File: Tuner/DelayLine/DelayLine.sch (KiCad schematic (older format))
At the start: 84 parts, among them J1 Conn_Coaxial, J10 Conn_Coaxial, J11 Conn_Coaxial, J12 Conn_Coaxial, J13 Conn_01x01, J14 Conn_01x01, J15 Conn_01x01, J16 Conn_01x01, J17 Conn_02x10_Odd_Even, J18 Conn_Coaxial, J19 Conn_Coaxial, J2 Conn_Coaxial, J20 Conn_Coaxial, J21 Conn_Coaxial, J22 Conn_Coaxial, J23 Conn_Coaxial, J24 Conn_Coaxial, J25 Conn_01x01, J26 Conn_01x01, J27 Conn_01x01, J28 Conn_01x01, J29 Conn_Coaxial, J3 Conn_Coaxial, J30 Conn_Coaxial, J31 Conn_Coaxial, J4 Conn_Coaxial, J5 Conn_Coaxial, J6 Conn_Coaxial, J7 Conn_Coaxial, J8 Conn_01x02, J9 Conn_01x02

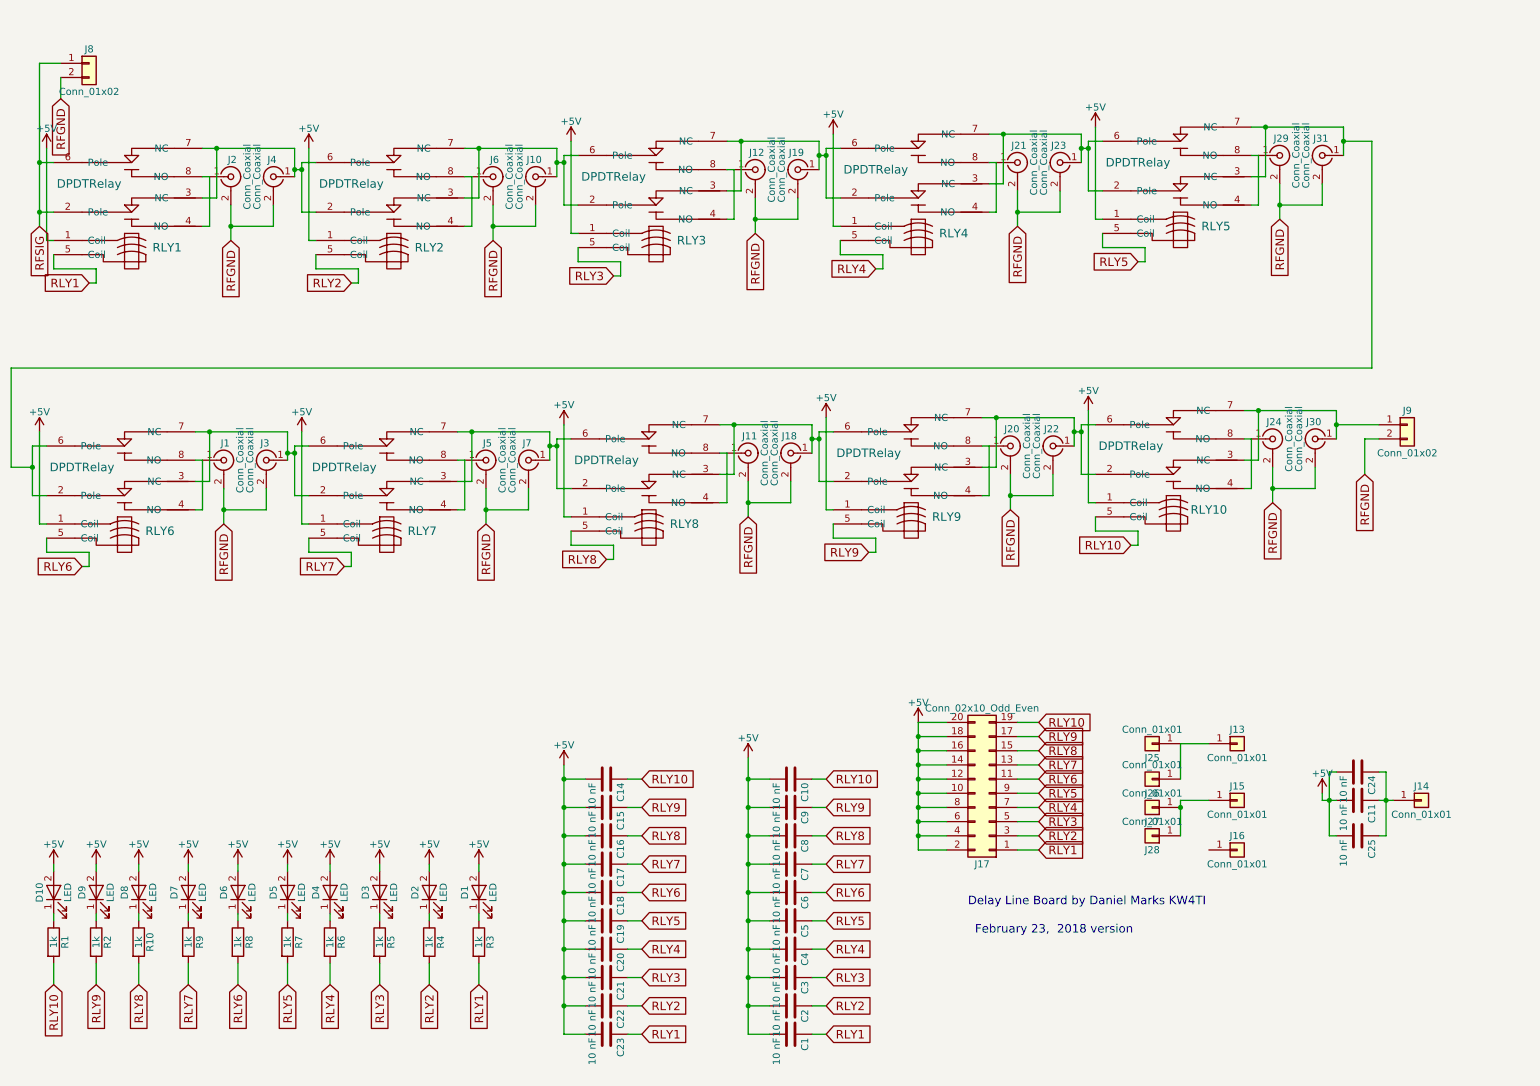
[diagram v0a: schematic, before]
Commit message: Added phase reversal transformer
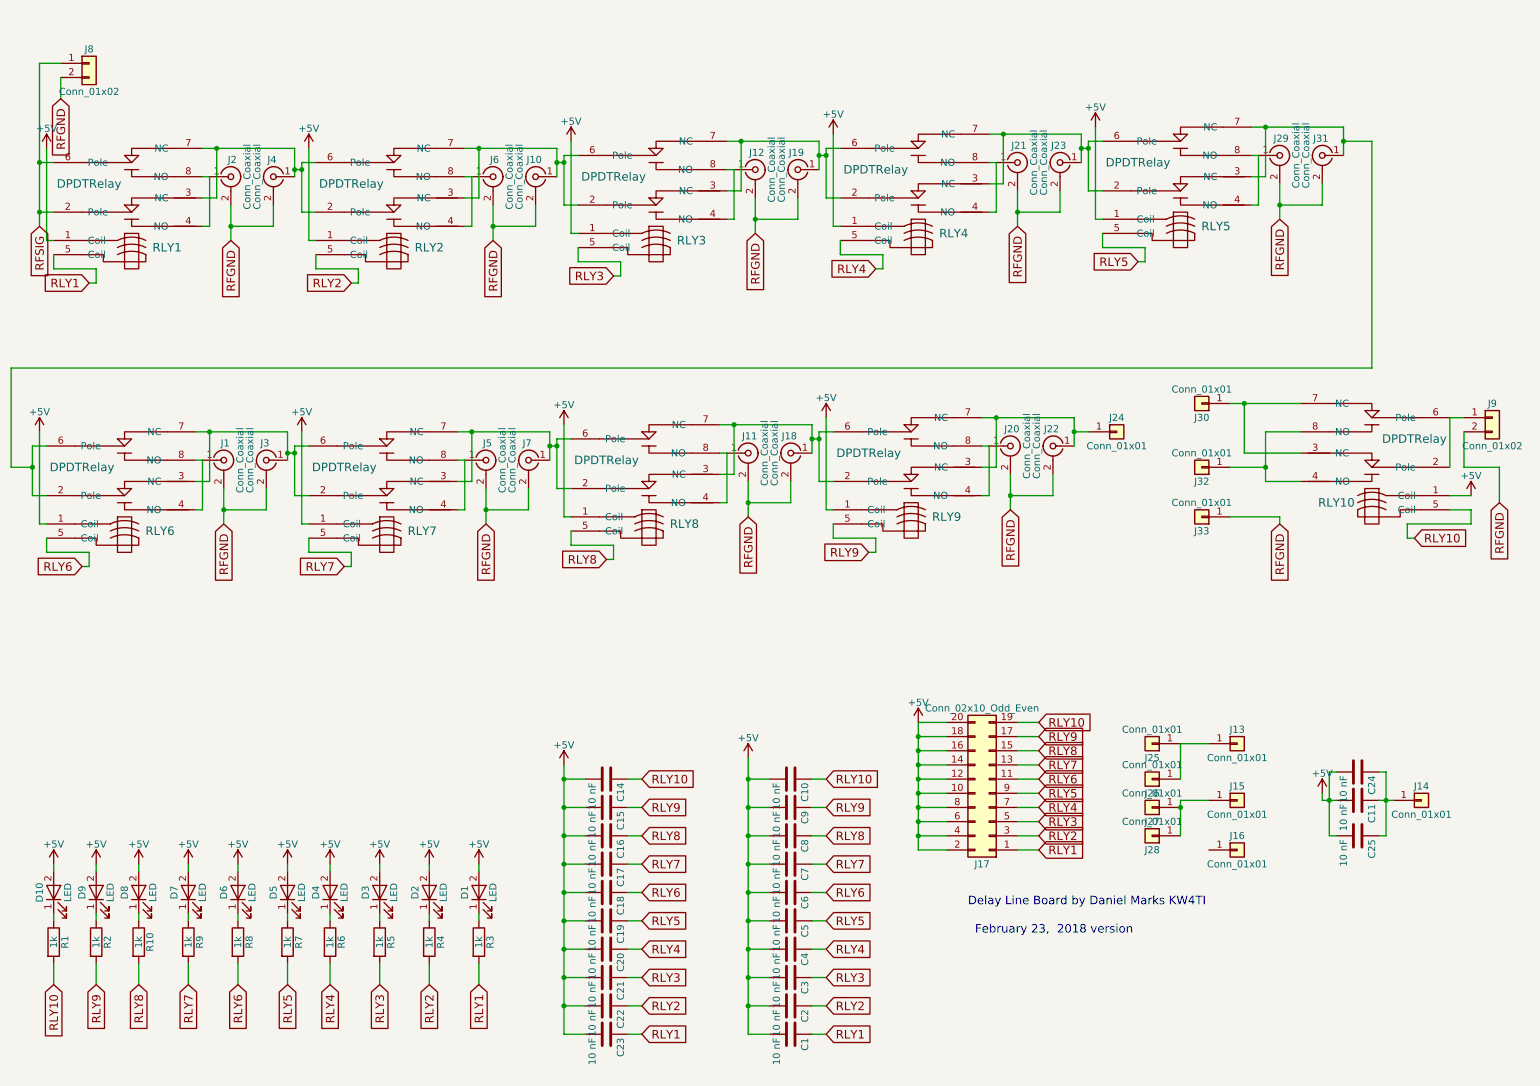
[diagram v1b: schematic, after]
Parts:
- removed J24, J30: Conn_Coaxial, Connectors:bnc-ci, symbol Conn_Coaxial
- added J24, J30, J32, J33: Conn_01x01, Connectors:1pin, symbol Conn_01x01
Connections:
- net RFGND: now also J33.1 (Pin_1)
- net at RLY10.3 (NC), RLY10.7 (NC): now also J30.1 (Pin_1); no longer J9.1 (Pin_1)
- net at J22.1 (In), RLY9.3 (NC), RLY9.7 (NC): now also J24.1 (Pin_1); no longer RLY10.2 (Pole), RLY10.6 (Pole)
- net at RLY10.4 (NO), RLY10.8 (NO): now also J32.1 (Pin_1)
- new net: J9.1 (Pin_1), RLY10.2 (Pole), RLY10.6 (Pole)
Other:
- moved on the sheet: J9, RLY10

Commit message: Added Quad Coupler
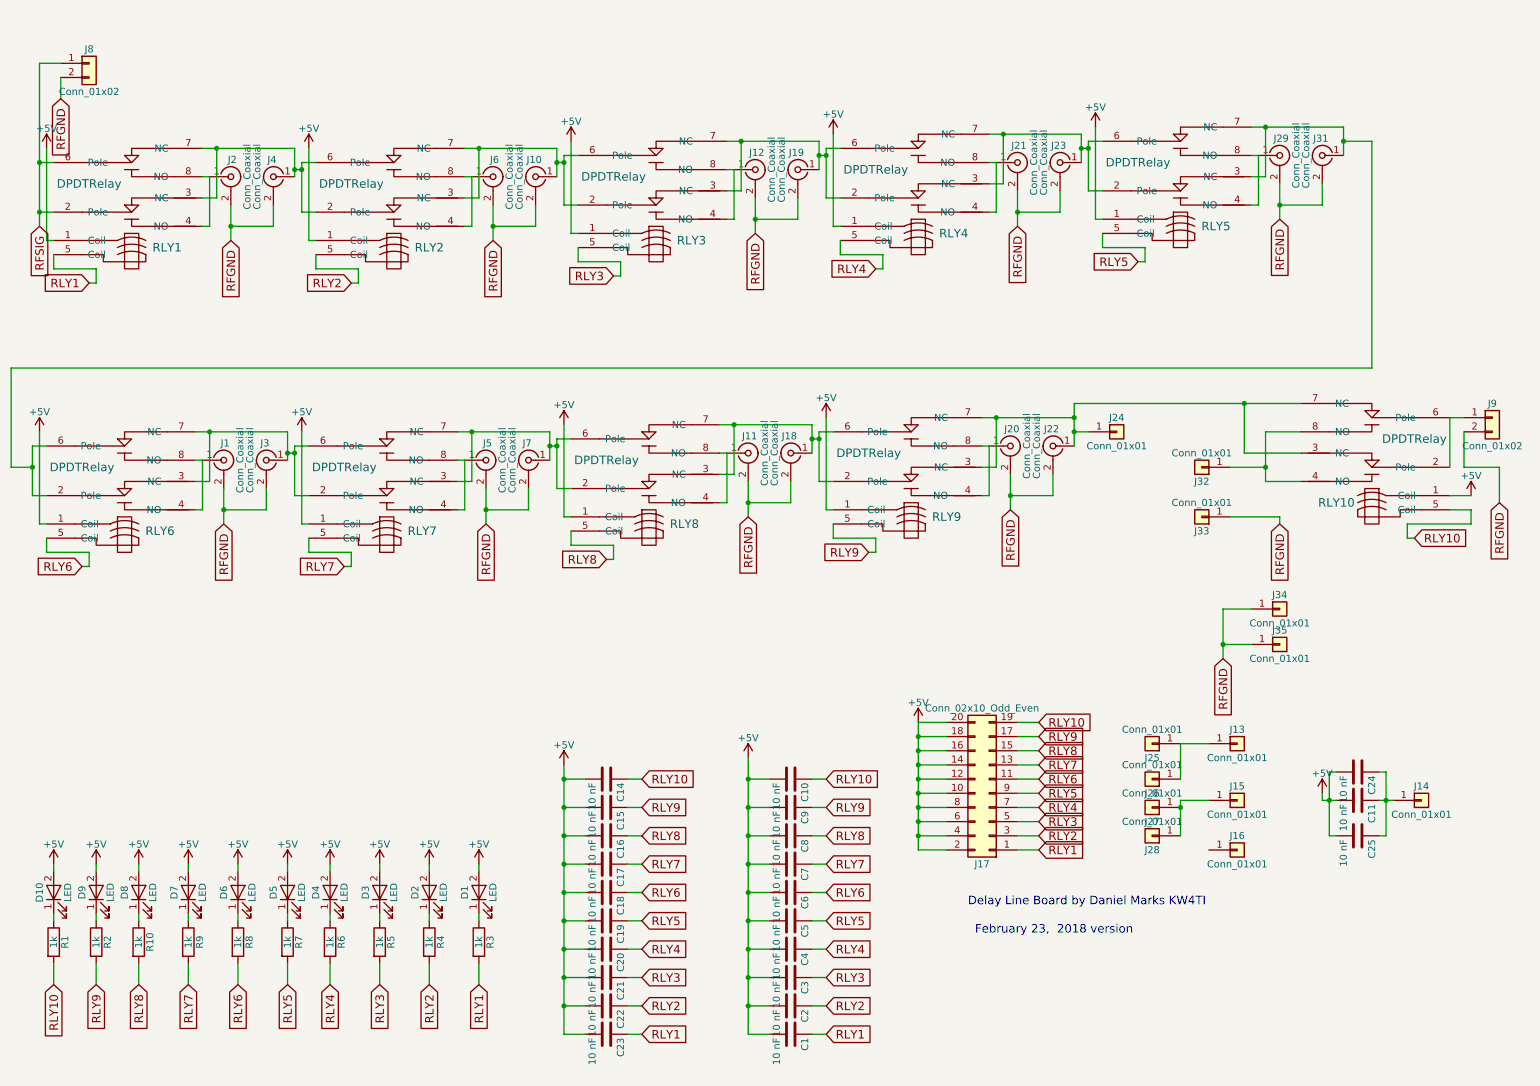
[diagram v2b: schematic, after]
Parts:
- removed J30: Conn_01x01, Connectors:1pin, symbol Conn_01x01
- added J34, J35: Conn_01x01, tuner:SOLDERJUMPER, symbol Conn_01x01
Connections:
- net RFGND: now also J34.1 (Pin_1), J35.1 (Pin_1)
- net at J22.1 (In), J24.1 (Pin_1), RLY9.3 (NC)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: now also RLY10.3 (NC), RLY10.7 (NC)

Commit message: Modified DelayLine to include bypass control
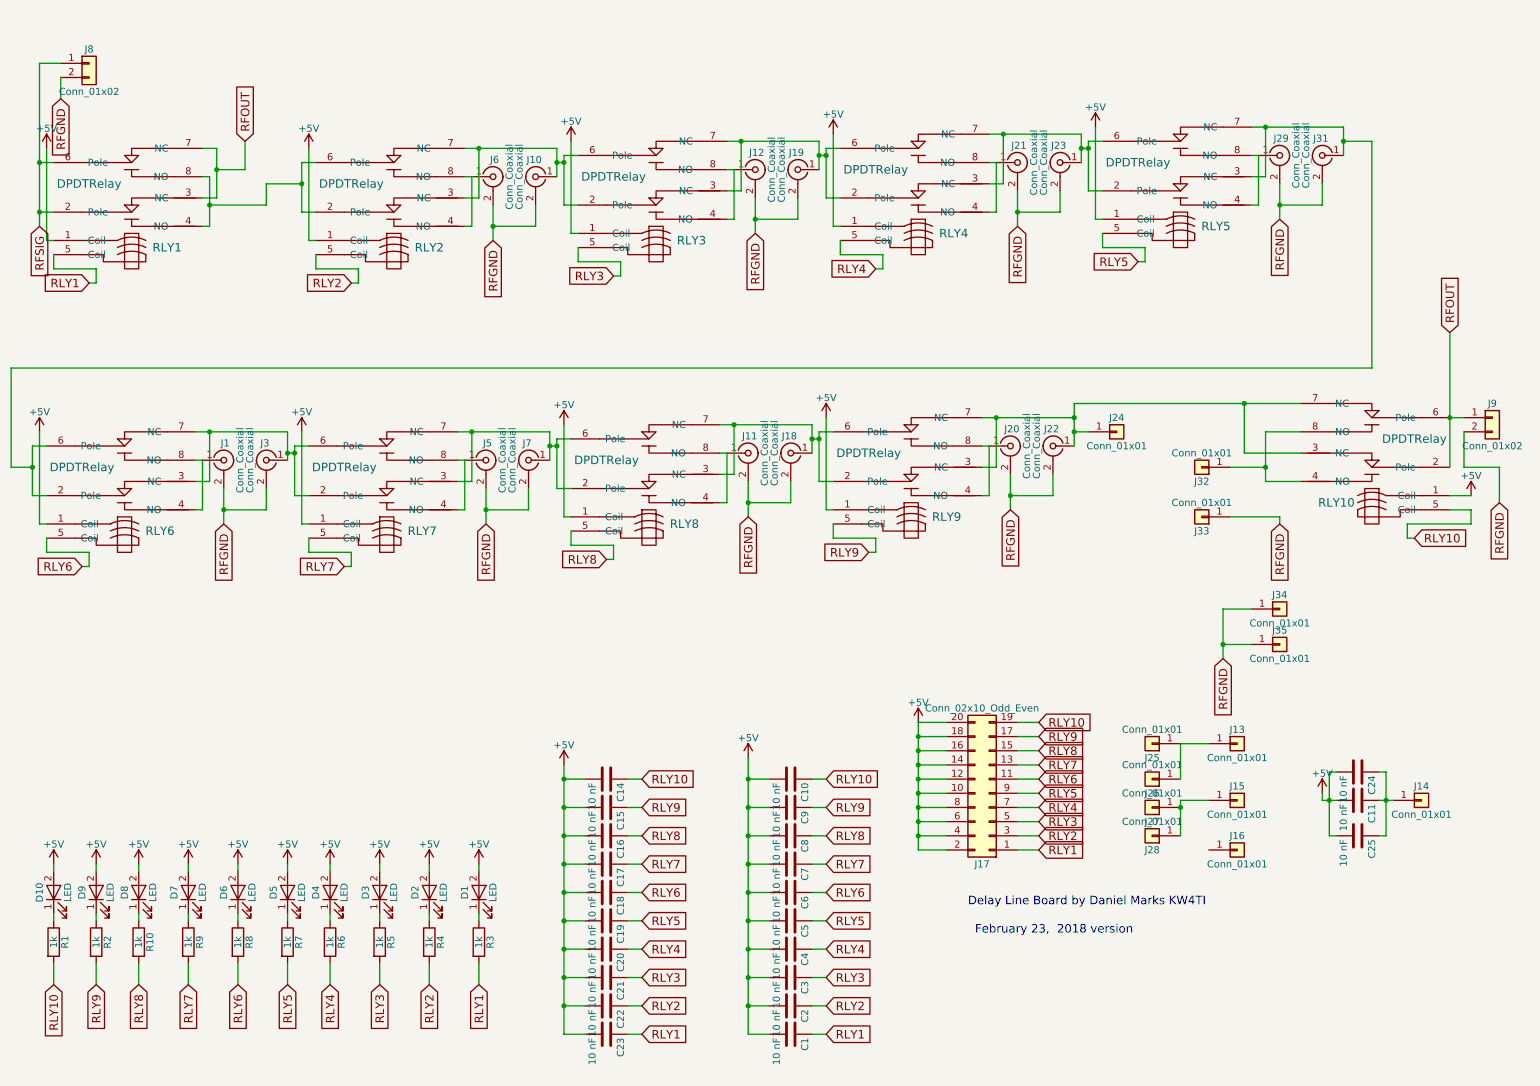
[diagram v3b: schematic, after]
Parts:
- removed J2, J4: Conn_Coaxial, Connectors:bnc-ci, symbol Conn_Coaxial
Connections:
- net RFOUT: now reaches J9.1 (Pin_1), RLY10.2 (Pole), RLY10.6 (Pole)
- net RFOUT: now also RLY1.3 (NC), RLY1.7 (NC)
- net at RLY2.2 (Pole), RLY2.6 (Pole): now also RLY1.4 (NO), RLY1.8 (NO); no longer RLY1.3 (NC), RLY1.7 (NC)
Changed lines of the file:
@@
 	1    0    0    -1
 $EndComp
-$Comp
-L Conn_Coaxial J2
-U 1 1 5C72CAE2
-P 2100 1550
-F 0 "J2" H 2110 1670 50  0000 C CNN
-F 1 "Conn_Coaxial" V 2215 1550 50  0000 C CNN
-F 2 "Connectors:bnc-ci" H 2100 1550 50  0001 C CNN
-F 3 "" H 2100 1550 50  0001 C CNN
-	1    2100 1550
-	1    0    0    -1
-$EndComp
-$Comp
-L Conn_Coaxial J4
-U 1 1 5C72CCE7
-P 2400 1550
-F 0 "J4" H 2410 1670 50  0000 C CNN
-F 1 "Conn_Coaxial" V 2515 1550 50  0000 C CNN
-F 2 "Connectors:bnc-ci" H 2400 1550 50  0001 C CNN
-F 3 "" H 2400 1550 50  0001 C CNN
-	1    2400 1550
-	-1   0    0    -1
-$EndComp
-Text GLabel 2100 2000 3    60   Input ~ 0
-RFGND
 Text GLabel 2950 2300 0    60   Input ~ 0
 RLY2
@@
 Text GLabel 9500 4000 3    60   Input ~ 0
 RFGND
-Connection ~ 2100 1900
-Wire Wire Line
-	2400 1900 2400 1750
-Wire Wire Line
-	2100 1900 2400 1900
-Wire Wire Line
-	2100 1750 2100 2000
 Wire Wire Line
 	750  1800 850  1800
@@
 	2000 1700 2000 1350
 Wire Wire Line
-	1900 1350 2550 1350
+	2000 1350 1900 1350
 Wire Wire Line
 	1950 1550 1900 1550
@@
 Wire Wire Line
 	1950 1900 1900 1900
-Wire Wire Line
-	2550 1350 2550 1550
-Connection ~ 2000 1350
 Wire Wire Line
 	800  1350 800  2000
@@
 Wire Wire Line
 	2600 1450 2600 1800
-Wire Wire Line
-	2600 1500 2550 1500
-Connection ~ 2550 1500
-Connection ~ 2600 1500
 Connection ~ 5800 1850
 Wire Wire Line
@@
 	10800 3600 10800 3350
 Wire Wire Line
-	10700 3600 10700 3250
+	10700 2650 10700 3600
 Wire Wire Line
 	10700 3250 10800 3250
@@
 Connection ~ 9100 4850
 Connection ~ 8050 3250
+Text GLabel 10700 2650 1    60   Input ~ 0
+RFOUT
+Connection ~ 10700 3250
+Wire Wire Line
+	1950 1750 2350 1750
+Wire Wire Line
+	2350 1750 2350 1600
+Wire Wire Line
+	2350 1600 2600 1600
+Connection ~ 2600 1600
+Connection ~ 1950 1750
+Text GLabel 2200 1300 1    60   Input ~ 0
+RFOUT
+Wire Wire Line
+	2200 1300 2200 1500
+Wire Wire Line
+	2200 1500 2000 1500
+Connection ~ 2000 1500
 $EndSCHEMATC

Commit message: Changed DelayLine to short out sections
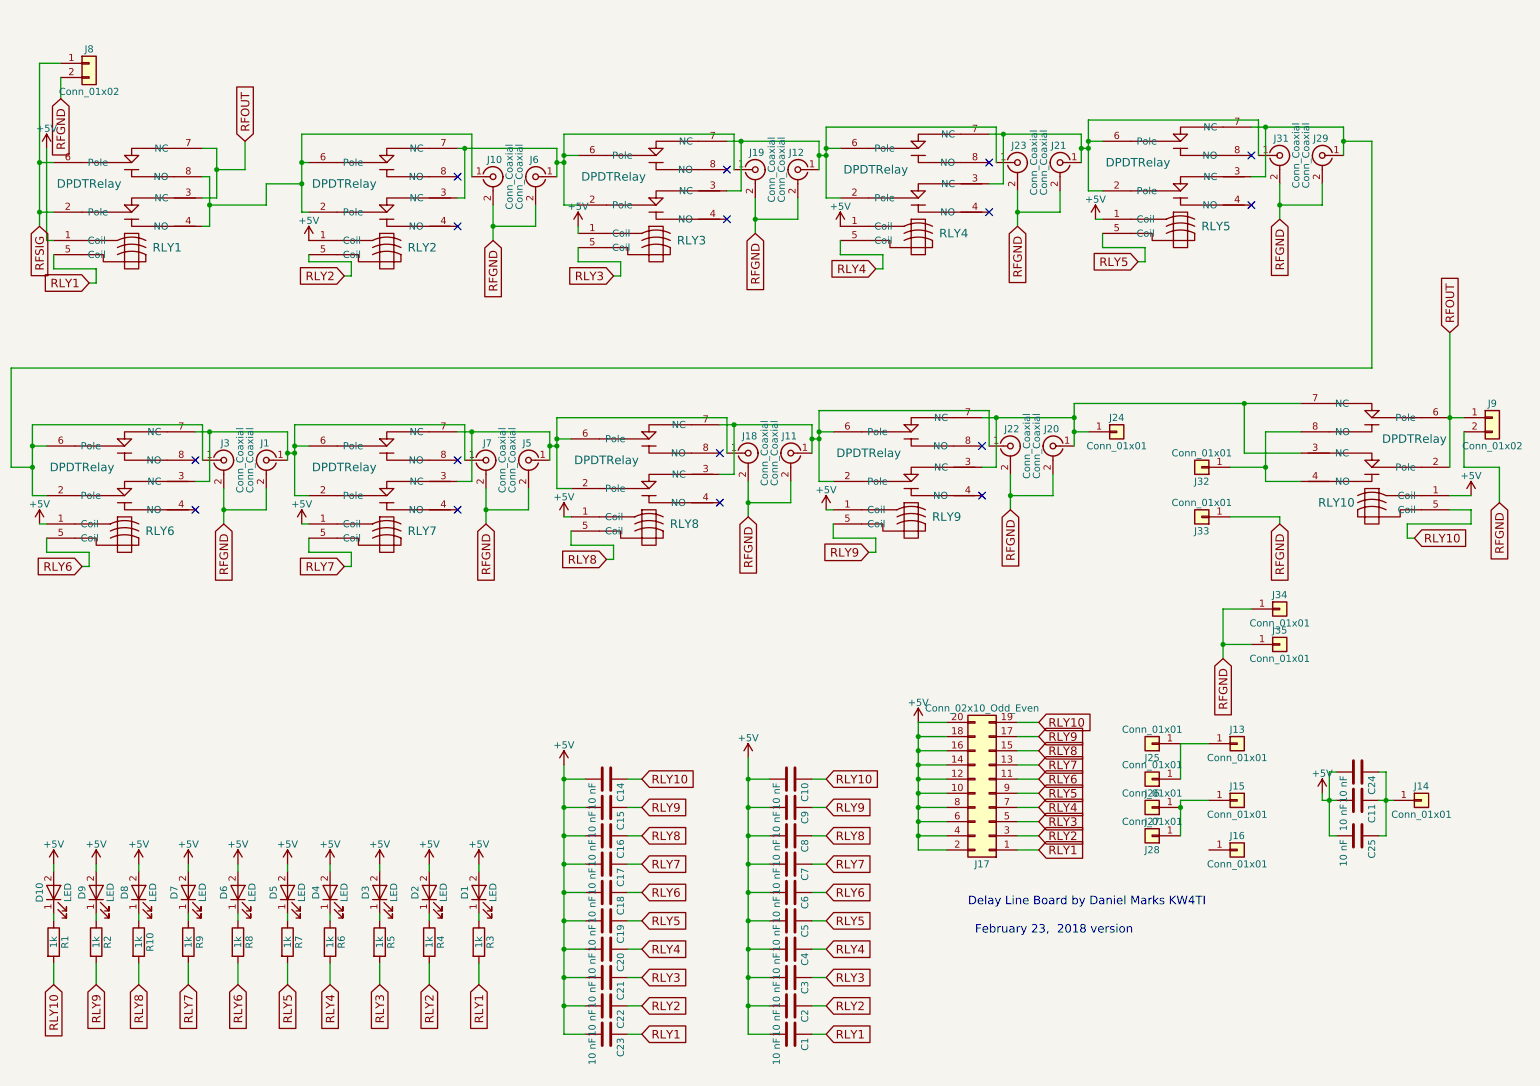
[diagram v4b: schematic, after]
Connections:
- net at RLY1.4 (NO), RLY1.8 (NO), RLY2.2 (Pole)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: now also J10.1 (In)
- net at J24.1 (Pin_1), RLY10.3 (NC), RLY10.7 (NC)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: now also J20.1 (In); no longer J22.1 (In)
- net at RLY2.3 (NC), RLY2.7 (NC), RLY3.2 (Pole)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: now also J19.1 (In), J6.1 (In); no longer J10.1 (In)
- net at RLY3.3 (NC), RLY3.7 (NC), RLY4.2 (Pole)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: now also J12.1 (In), J23.1 (In); no longer J19.1 (In)
- net at RLY4.3 (NC), RLY4.7 (NC), RLY5.2 (Pole)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: now also J21.1 (In), J31.1 (In); no longer J23.1 (In)
- net at RLY5.3 (NC), RLY5.7 (NC), RLY6.2 (Pole)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: now also J29.1 (In), J3.1 (In); no longer J31.1 (In)
- net at RLY6.3 (NC), RLY6.7 (NC), RLY7.2 (Pole)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: now also J1.1 (In), J7.1 (In); no longer J3.1 (In)
- net at RLY7.3 (NC), RLY7.7 (NC), RLY8.2 (Pole)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: now also J18.1 (In), J5.1 (In); no longer J7.1 (In)
- net at RLY8.3 (NC), RLY8.7 (NC), RLY9.2 (Pole)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: now also J11.1 (In), J22.1 (In); no longer J18.1 (In)
- now unconnected: RLY2.4 (NO), RLY2.8 (NO), RLY3.4 (NO), RLY3.8 (NO), RLY4.4 (NO), RLY4.8 (NO), RLY5.4 (NO), RLY5.8 (NO), RLY6.4 (NO), RLY6.8 (NO), RLY7.4 (NO), RLY7.8 (NO), RLY8.4 (NO), RLY8.8 (NO), RLY9.4 (NO), RLY9.8 (NO)
- no-connect marks 0 -> 16
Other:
- moved on the sheet: J1, J10, J11, J12, J18, J19, J20, J21, J22, J23, J29, J3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
